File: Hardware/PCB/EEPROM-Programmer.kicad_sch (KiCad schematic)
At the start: 14 parts, among them U1 74HC00, U10 74HC595, U11 74HC595, U12 74HC595, U13 MCP2221AxP, U2 74HC04, U3 74HC08, U4 74HC08, U5 74HC08, U6 74LS32, U7 74HC393, U8 74HC393, U9 74HC165

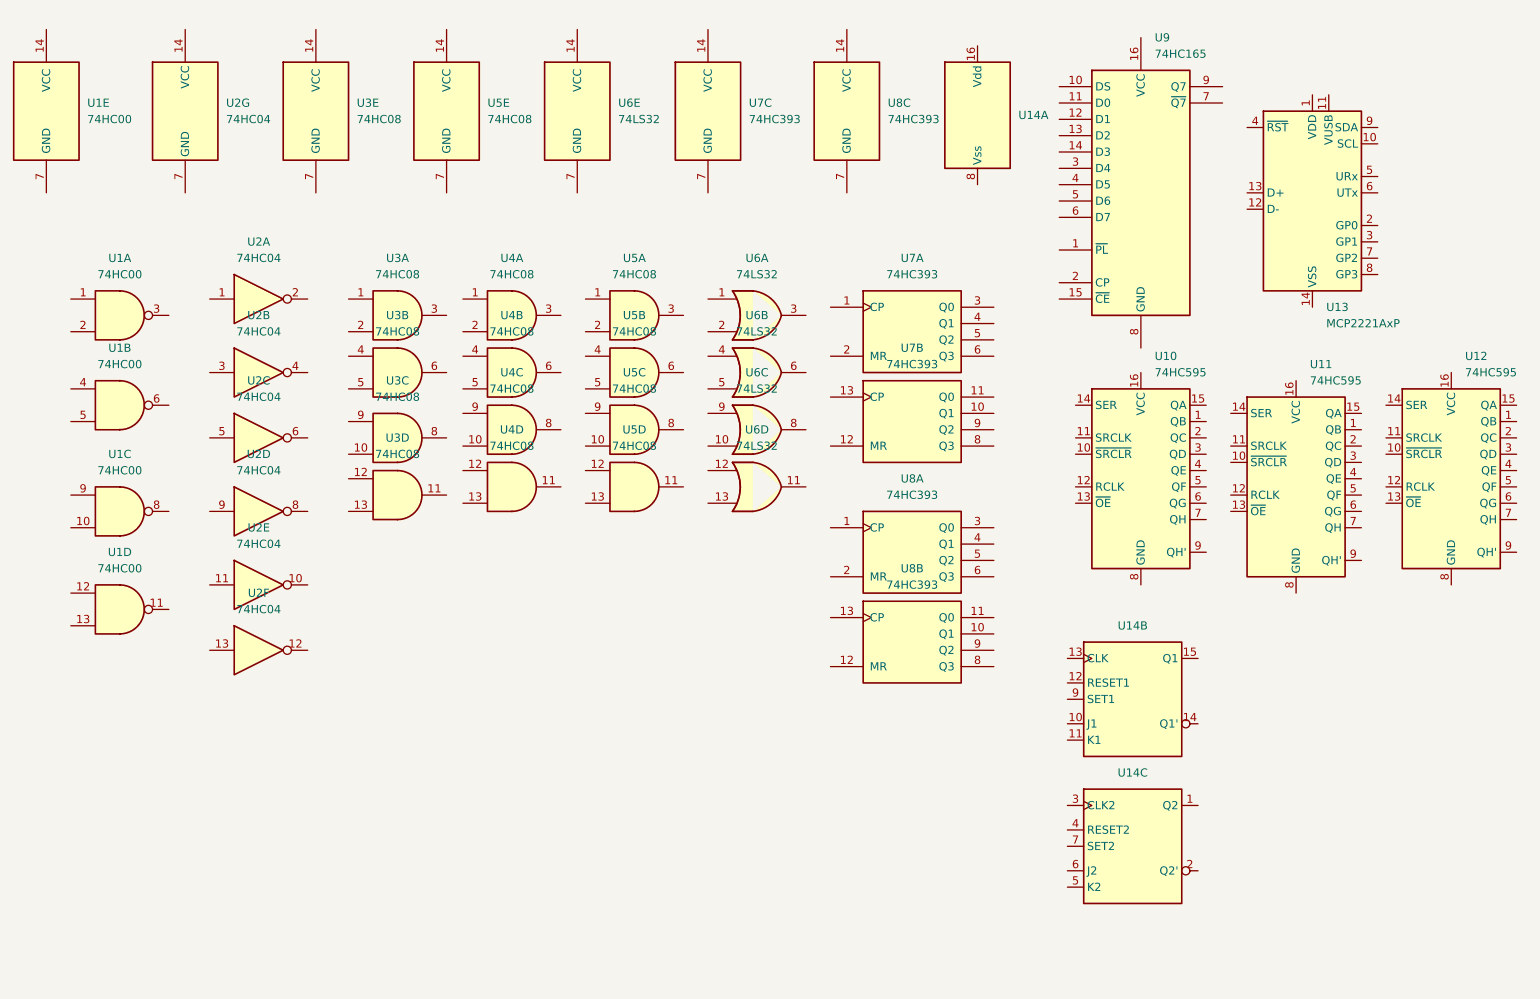
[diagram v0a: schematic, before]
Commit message: state machine added to schemaatic
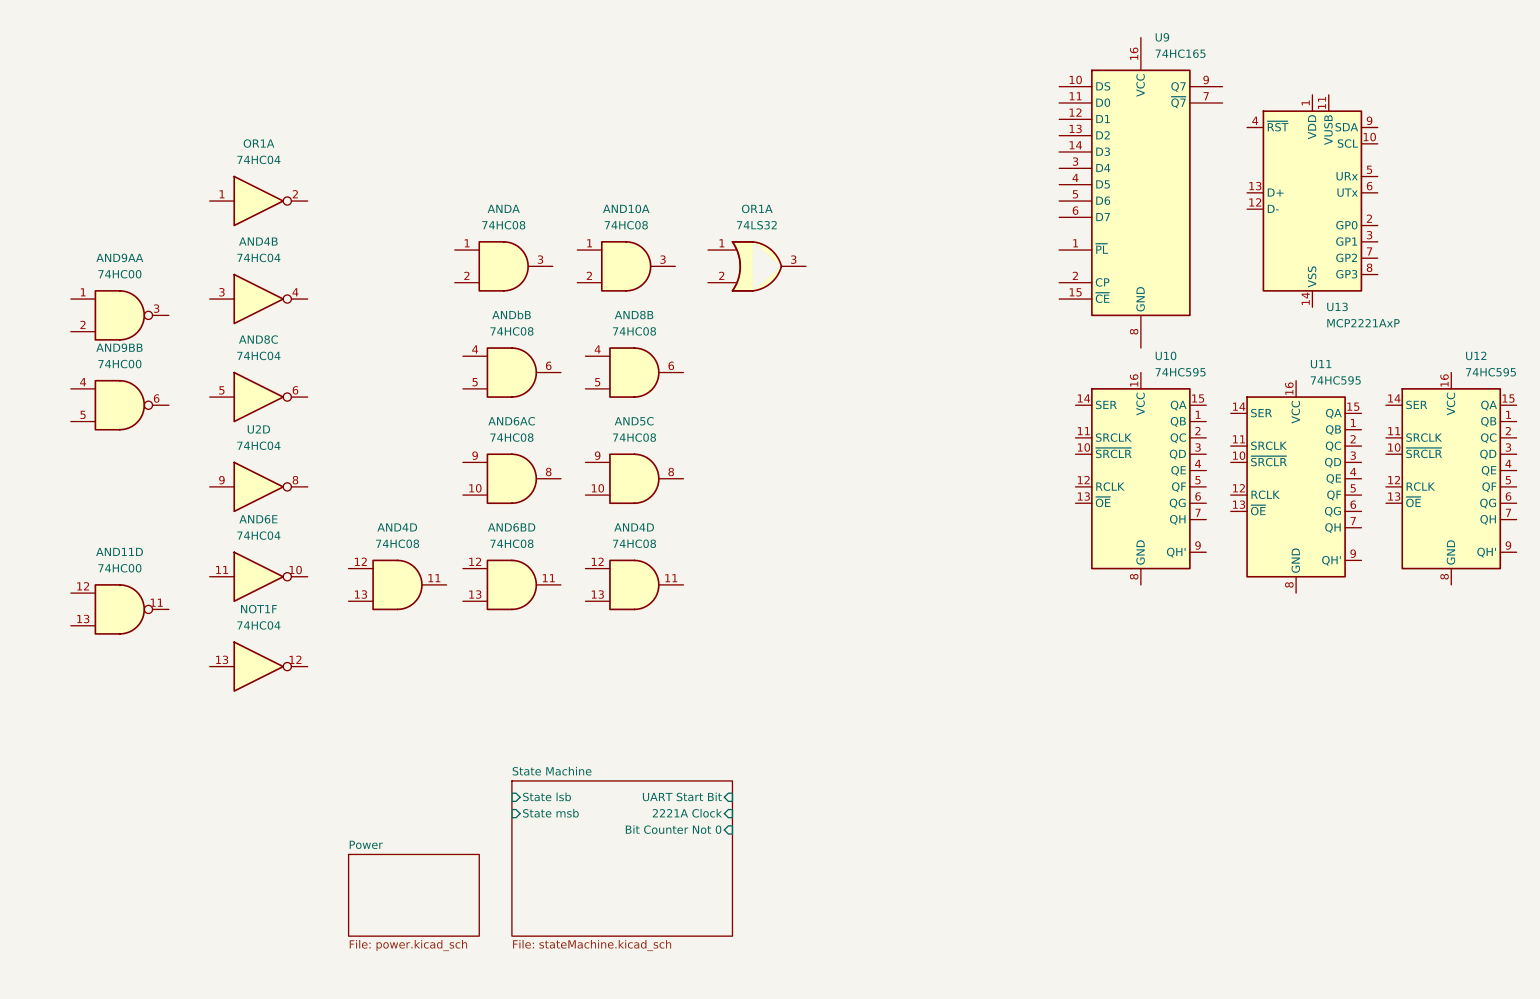
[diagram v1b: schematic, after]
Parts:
- removed unit 3 of U1
- removed unit 5 of U1
- removed U14: (no value), symbol custom:CD4027B
- removed unit 7 of U2
- removed unit 3 of U3
- removed unit 1 of U3
- removed unit 2 of U3
- removed unit 5 of U3
- removed unit 5 of U5
- removed unit 3 of U6
- removed unit 2 of U6
- removed unit 5 of U6
- removed unit 4 of U6
- removed U7, U8: 74HC393, symbol 74xx:74LS393
- renumbered U4 to AND, U5 to AND10, U1 to AND11, U5 to AND4, U3 to AND4, U2 to AND4, U5 to AND5, U2 to AND6, U4 to AND6A, U4 to AND6B, U2 to AND8, U5 to AND8, U1 to AND9A, U1 to AND9B, U4 to ANDb, U2 to NOT1, U2 to OR1, U6 to OR1
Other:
- added sheet Power (power.kicad_sch)
- added sheet State Machine (stateMachine.kicad_sch)
- moved on the sheet: AND10A, AND4B, AND4D, AND5C, AND6AC, AND6BD, AND6E, AND8C, ANDA, NOT1F, OR1A, U2D

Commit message: Writing maybe working, also started on other parts of schematic
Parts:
- removed AND10, AND4 (x2), AND5, AND6A, AND6B: 74HC08, symbol 74xx:74LS08
- removed AND11, AND9A, AND9B: 74HC00, Package_DIP:DIP-14_W7.62mm_Socket, symbol 74xx:74HC00
- removed AND6, AND8, NOT1, OR1: 74HC04, symbol 74xx:74HC04
- removed OR1: 74LS32, symbol 74xx:74LS32
- removed U10, U11, U12: 74HC595, symbol 74xx:74HC595
- removed U13: MCP2221AxP, Package_DIP:DIP-14_W7.62mm_Socket, symbol Interface_USB:MCP2221AxP
- removed U9: 74HC165, symbol 74xx:74HC165
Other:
- added sheet Data Handling (dataHandling.kicad_sch)
- added sheet Logic (logic.kicad_sch)
- moved on the sheet: ANDA, ANDbB, U2D

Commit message: Finished schematic
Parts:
- removed AND, ANDb: 74HC08, symbol 74xx:74LS08
- removed U2: 74HC04, symbol 74xx:74HC04
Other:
- removed sheet Logic
- sheet Data Handling ports: added Command Finished, EEPROM Output Enable, EEPROM Write Enable, Is Sending, MCP2221A Clock, R~{W} EEPROM, Set UART Activity, Shift In Clock, Start Sending, ~{Start Sending}; removed none
- sheet State Machine ports: added Command Finished, EEPROM Output Enable, EEPROM Write Enable, Is Sending, R~{W} EEPROM, Set UART Activity, Shift In Clock, Start Sending, ~{Start Sending}; removed Bit Counter Not 0, State lsb, State msb, UART Start Bit
